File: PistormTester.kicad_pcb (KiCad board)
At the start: 2 copper layers, 100.1 x 99.8 mm, 88 parts, among them J1 USB_B_Micro, J2 Conn_02x12_Odd_Even, J3 Conn_01x06_Female, J4 Conn_01x16_Female, J5 Conn_01x16_Female, J6 Conn_01x16_Female, J7 Conn_02x13_Odd_Even, J8 Conn_01x13, J9 Conn_01x02, U2 68000D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

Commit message: initial checkin
Rev A as sent to JLC on 19/06/21
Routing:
- net /A12: track 29.2 -> 28.3 mm
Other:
- board text added: "@ABrugsch https://github.com/abrugsch/PistormTester"
- board text added: "Garbege Data Bus"
- board text removed: "@ABrugsch https://github.com/abrugsch/pistorm_tester"
- board text removed: "Data Bus"
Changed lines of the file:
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@@
     (thickness 1.6)
     (drawings 84)
-    (tracks 1120)
+    (tracks 1117)
     (zones 0)
     (modules 88)
@@
   (layers
     (0 F.Cu signal hide)
-    (31 B.Cu signal)
+    (31 B.Cu signal hide)
     (32 B.Adhes user)
     (33 F.Adhes user)
@@
       (outputformat 1)
       (mirror false)
-      (drillshape 1)
+      (drillshape 0)
       (scaleselection 1)
-      (outputdirectory ""))
+      (outputdirectory "production/gerbers/"))
   )
   (net 0 "")
@@
     (effects (font (size 1.5 1.5) (thickness 0.3)) (justify mirror))
   )
-  (gr_text "@ABrugsch\nhttps://github.com/abrugsch/pistorm_tester" (at 169.090886 153.035) (layer B.SilkS)
+  (gr_text "@ABrugsch\nhttps://github.com/abrugsch/PistormTester" (at 182.0672 150.8252) (layer B.SilkS)
     (effects (font (size 1.5 1.5) (thickness 0.3)) (justify left mirror))
   )
@@
     (effects (font (size 0.75 0.75) (thickness 0.1)) (justify right))
   )
-  (gr_text "Data Bus" (at 160.909 86.868 90) (layer F.SilkS)
-    (effects (font (size 1.2 1.2) (thickness 0.15)))
+  (gr_text " Garbege \nData Bus" (at 158.7754 86.7664 90) (layer F.SilkS)
+    (effects (font (size 1.5 1.5) (thickness 0.15)))
   )
   (gr_text VCC (at 100.965 94.488 270) (layer F.SilkS)
@@
   (segment (start 178.816 153.54018) (end 180.143989 152.212191) (width 0.25) (layer F.Cu) (net 14))
   (segment (start 178.816 153.797) (end 178.816 153.54018) (width 0.25) (layer F.Cu) (net 14))
-  (segment (start 165.608 142.24) (end 166.37 142.24) (width 0.25) (layer B.Cu) (net 15))
-  (segment (start 164.432999 143.415001) (end 165.608 142.24) (width 0.25) (layer B.Cu) (net 15))
-  (segment (start 154.051 143.415001) (end 164.432999 143.415001) (width 0.25) (layer B.Cu) (net 15))
-  (segment (start 153.6897 143.415001) (end 154.249401 143.415001) (width 0.25) (layer B.Cu) (net 15))
-  (segment (start 152.6047 144.500001) (end 153.6897 143.415001) (width 0.25) (layer B.Cu) (net 15))
-  (segment (start 151.714401 144.500001) (end 152.6047 144.500001) (width 0.25) (layer B.Cu) (net 15))
   (segment (start 175.26 143.256) (end 175.9965 143.256) (width 0.25) (layer F.Cu) (net 15))
   (segment (start 174.244 142.24) (end 175.26 143.256) (width 0.25) (layer F.Cu) (net 15))
   (segment (start 174.244 142.24) (end 166.37 142.24) (width 0.25) (layer F.Cu) (net 15))
+  (segment (start 165.608 142.24) (end 166.37 142.24) (width 0.25) (layer B.Cu) (net 15))
+  (segment (start 154.368951 143.5608) (end 164.2872 143.5608) (width 0.25) (layer B.Cu) (net 15))
+  (segment (start 164.2872 143.5608) (end 165.608 142.24) (width 0.25) (layer B.Cu) (net 15))
+  (segment (start 153.42975 144.500001) (end 154.368951 143.5608) (width 0.25) (layer B.Cu) (net 15))
+  (segment (start 151.714401 144.500001) (end 153.42975 144.500001) (width 0.25) (layer B.Cu) (net 15))
   (segment (start 159.385 139.7) (end 163.83 139.7) (width 0.25) (layer F.Cu) (net 16))
   (segment (start 157.124999 141.960001) (end 159.385 139.7) (width 0.25) (layer F.Cu) (net 16))
@@
   (segment (start 181.090978 143.727478) (end 181.090978 152.538022) (width 0.25) (layer F.Cu) (net 18))
   (segment (start 177.5715 140.208) (end 181.090978 143.727478) (width 0.25) (layer F.Cu) (net 18))
-  (segment (start 165.194999 140.875001) (end 166.37 139.7) (width 0.25) (layer B.Cu) (net 19))
-  (segment (start 162.973001 140.875001) (end 165.194999 140.875001) (width 0.25) (layer B.Cu) (net 19))
-  (segment (start 161.486 139.420001) (end 162.941 140.875001) (width 0.25) (layer B.Cu) (net 19))
-  (segment (start 151.714401 139.420001) (end 161.486 139.420001) (width 0.25) (layer B.Cu) (net 19))
   (segment (start 175.133 140.208) (end 175.9965 140.208) (width 0.25) (layer F.Cu) (net 19))
   (segment (start 174.625 139.7) (end 175.133 140.208) (width 0.25) (layer F.Cu) (net 19))
   (segment (start 174.625 139.7) (end 166.37 139.7) (width 0.25) (layer F.Cu) (net 19))
+  (segment (start 165.1 140.97) (end 166.37 139.7) (width 0.25) (layer B.Cu) (net 19))
+  (segment (start 153.2644 140.97) (end 165.1 140.97) (width 0.25) (layer B.Cu) (net 19))
+  (segment (start 151.714401 139.420001) (end 153.2644 140.97) (width 0.25) (layer B.Cu) (net 19))
   (segment (start 163.550001 136.880001) (end 163.83 137.16) (width 0.25) (layer F.Cu) (net 20))
   (segment (start 151.714401 136.880001) (end 163.550001 136.880001) (width 0.25) (layer F.Cu) (net 20))
@@
   (segment (start 165.194999 135.795001) (end 166.37 134.62) (width 0.25) (layer B.Cu) (net 27))
   (segment (start 162.465001 135.795001) (end 165.194999 135.795001) (width 0.25) (layer B.Cu) (net 27))
-  (segment (start 153.009001 130.784001) (end 158.020001 135.795001) (width 0.25) (layer B.Cu) (net 27))
-  (segment (start 153.009001 129.260001) (end 153.009001 130.784001) (width 0.25) (layer B.Cu) (net 27))
-  (segment (start 158.020001 135.795001) (end 162.941 135.795001) (width 0.25) (layer B.Cu) (net 27))
-  (segment (start 151.714401 129.260001) (end 153.009001 129.260001) (width 0.25) (layer B.Cu) (net 27))
   (segment (start 175.1075 134.62) (end 175.9965 133.731) (width 0.25) (layer F.Cu) (net 27))
   (segment (start 175.1075 134.62) (end 166.37 134.62) (width 0.25) (layer F.Cu) (net 27))
+  (segment (start 158.959801 135.795001) (end 162.941 135.795001) (width 0.25) (layer B.Cu) (net 27))
+  (segment (start 152.424801 129.260001) (end 158.959801 135.795001) (width 0.25) (layer B.Cu) (net 27))
+  (segment (start 151.714401 129.260001) (end 152.424801 129.260001) (width 0.25) (layer B.Cu) (net 27))
   (segment (start 159.385 132.08) (end 163.83 132.08) (width 0.25) (layer F.Cu) (net 28))
   (segment (start 154.025001 126.720001) (end 159.385 132.08) (width 0.25) (layer F.Cu) (net 28))
@@
   (segment (start 174.5995 132.08) (end 175.9965 130.683) (width 0.25) (layer F.Cu) (net 31))
   (segment (start 174.5995 132.08) (end 166.37 132.08) (width 0.25) (layer F.Cu) (net 31))
-  (segment (start 154.813 127.2786) (end 151.714401 124.180001) (width 0.25) (layer B.Cu) (net 31))
-  (segment (start 154.813 127.381) (end 154.813 127.2786) (width 0.25) (layer B.Cu) (net 31))
-  (segment (start 160.687001 133.255001) (end 154.813 127.381) (width 0.25) (layer B.Cu) (net 31))
+  (segment (start 151.714401 124.282401) (end 151.714401 124.180001) (width 0.25) (layer B.Cu) (net 31))
+  (segment (start 160.687001 133.255001) (end 151.714401 124.282401) (width 0.25) (layer B.Cu) (net 31))
   (segment (start 163.576 133.255001) (end 160.687001 133.255001) (width 0.25) (layer B.Cu) (net 31))
   (segment (start 174.440499 130.715001) (end 175.9965 129.159) (width 0.25) (layer F.Cu) (net 32))
@@
   (segment (start 89.869043 99.623428) (end 89.869043 103.483543) (width 0.25) (layer F.Cu) (net 100))
   (via (at 105.57399 85.724999) (size 0.8) (drill 0.4) (layers F.Cu B.Cu) (net 101))
-  (segment (start 118.085399 85.724999) (end 105.57399 85.724999) (width 0.25) (layer B.Cu) (net 101))
-  (segment (start 118.440401 86.080001) (end 118.085399 85.724999) (width 0.25) (layer B.Cu) (net 101))
-  (segment (start 128.854401 86.080001) (end 118.440401 86.080001) (width 0.25) (layer B.Cu) (net 101))
   (segment (start 93.425033 70.912967) (end 95.598999 68.739001) (width 0.25) (layer F.Cu) (net 101))
   (segment (start 95.492978 94.112244) (end 93.425033 92.0443) (width 0.25) (layer F.Cu) (net 101))
@@
   (segment (start 105.329967 72.309967) (end 105.329967 81.582377) (width 0.25) (layer F.Cu) (net 101))
   (segment (start 101.759001 68.739001) (end 105.329967 72.309967) (width 0.25) (layer F.Cu) (net 101))
-  (segment (start 128.854401 88.620001) (end 118.211001 88.620001) (width 0.25) (layer B.Cu) (net 102))
-  (segment (start 118.440401 88.620001) (end 118.211001 88.620001) (width 0.25) (layer B.Cu) (net 102))
+  (segment (start 105.867199 85.724999) (end 105.57399 85.724999) (width 0.25) (layer B.Cu) (net 101))
+  (segment (start 106.222201 86.080001) (end 105.867199 85.724999) (width 0.25) (layer B.Cu) (net 101))
+  (segment (start 128.854401 86.080001) (end 106.222201 86.080001) (width 0.25) (layer B.Cu) (net 101))
   (segment (start 97.187001 66.388999) (end 98.552 65.024) (width 0.25) (layer F.Cu) (net 102))
   (segment (start 95.042967 94.298644) (end 92.975022 92.2307) (width 0.25) (layer F.Cu) (net 102))
@@
   (via (at 106.23439 86.8079) (size 0.8) (drill 0.4) (layers F.Cu B.Cu) (net 102))
   (segment (start 105.779978 70.346978) (end 105.779978 81.395978) (width 0.25) (layer F.Cu) (net 102))
-  (segment (start 108.046491 88.620001) (end 106.23439 86.8079) (width 0.25) (layer B.Cu) (net 102))
   (segment (start 106.298997 86.743293) (end 106.23439 86.8079) (width 0.25) (layer F.Cu) (net 102))
-  (segment (start 118.211001 88.620001) (end 108.046491 88.620001) (width 0.25) (layer B.Cu) (net 102))
   (segment (start 106.298997 81.914997) (end 106.298997 86.743293) (width 0.25) (layer F.Cu) (net 102))
   (segment (start 105.779978 81.395978) (end 106.298997 81.914997) (width 0.25) (layer F.Cu) (net 102))
@@
   (segment (start 98.552 65.024) (end 99.727001 66.199001) (width 0.25) (layer F.Cu) (net 102))
   (segment (start 101.632001 66.199001) (end 105.779978 70.346978) (width 0.25) (layer F.Cu) (net 102))
+  (segment (start 128.854401 88.620001) (end 128.828402 88.646) (width 0.25) (layer B.Cu) (net 102))
+  (segment (start 106.24369 86.8172) (end 106.23439 86.8079) (width 0.25) (layer B.Cu) (net 102))
+  (segment (start 127.0508 86.8172) (end 106.24369 86.8172) (width 0.25) (layer B.Cu) (net 102))
+  (segment (start 128.853601 88.620001) (end 127.0508 86.8172) (width 0.25) (layer B.Cu) (net 102))
+  (segment (start 128.854401 88.620001) (end 128.853601 88.620001) (width 0.25) (layer B.Cu) (net 102))
   (segment (start 90.319054 102.409554) (end 91.5415 103.632) (width 0.25) (layer F.Cu) (net 103))
   (segment (start 90.319054 99.809828) (end 90.319054 102.409554) (width 0.25) (layer F.Cu) (net 103))

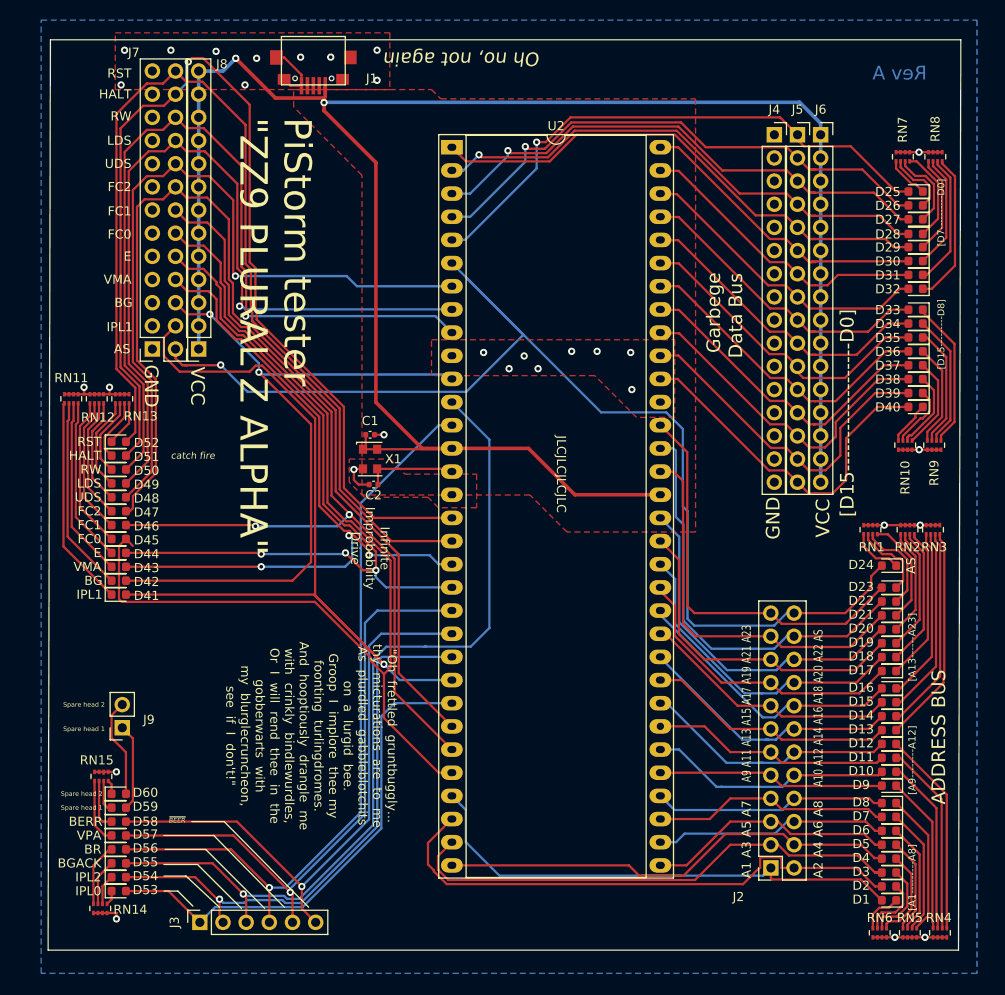
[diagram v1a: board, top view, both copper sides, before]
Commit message: Rev B tweaks to layout
cleaned up front pours and track routes
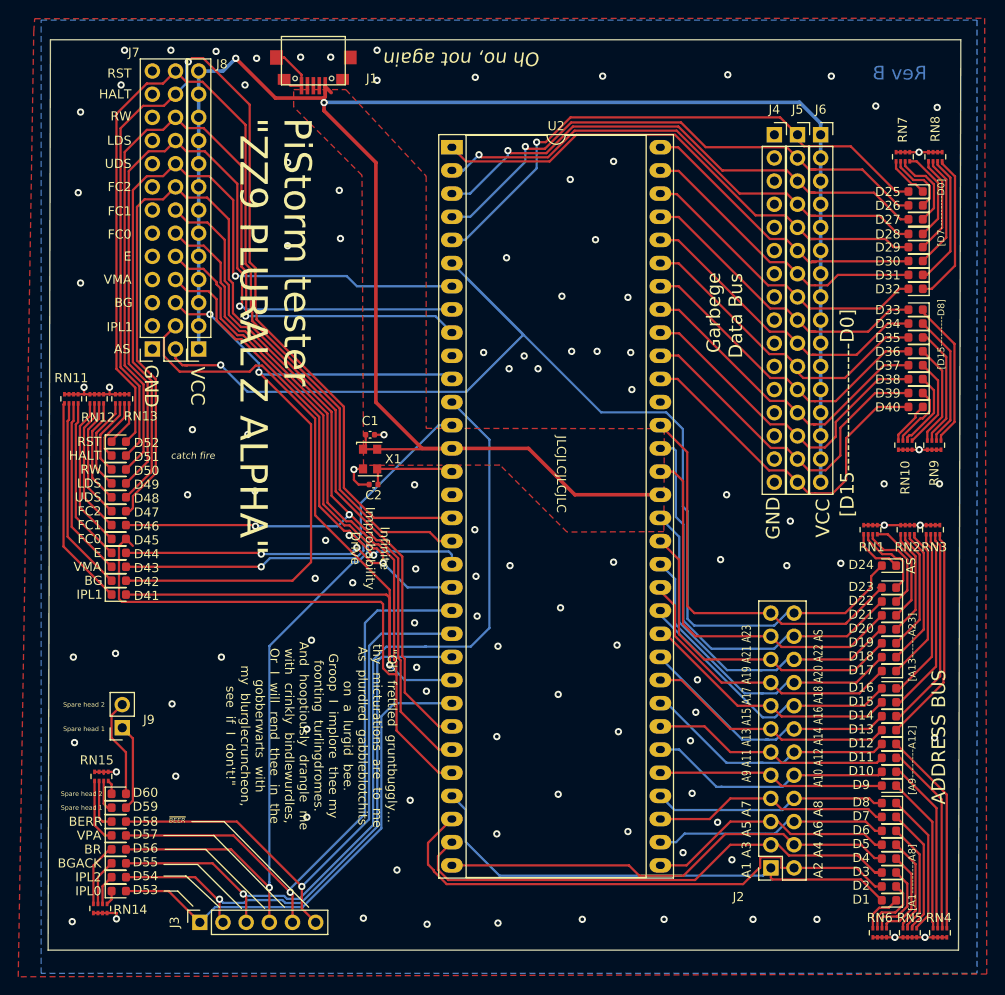
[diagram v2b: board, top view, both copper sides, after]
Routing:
- net /FC0: track 115.5 -> 120.5 mm
- net /IPL1: track 93.5 -> 98.1 mm
- net /VMA: track 79.5 -> 81.6 mm
- net /FC1: track 98.6 -> 99.7 mm
- net +5V: track 226.5 -> 227.5 mm
- net /FC2: track 114.4 -> 115.3 mm
- net GND: vias 30 -> 109
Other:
- board text added: "Rev B"
- board text removed: "Rev A"
